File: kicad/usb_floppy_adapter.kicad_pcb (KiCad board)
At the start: 2 copper layers, 48 x 19 mm, 26 parts, among them J1 Conn_02x17_Odd_Even, J2 MICRO_USB_B, J3 Conn_01x02, J4 Conn_01x04, J5 GS2, J6 GS2, J7 GS3, U1 LM1117-3.3, U2 STM32F103C8Tx, U3 USBLC6-2SC6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

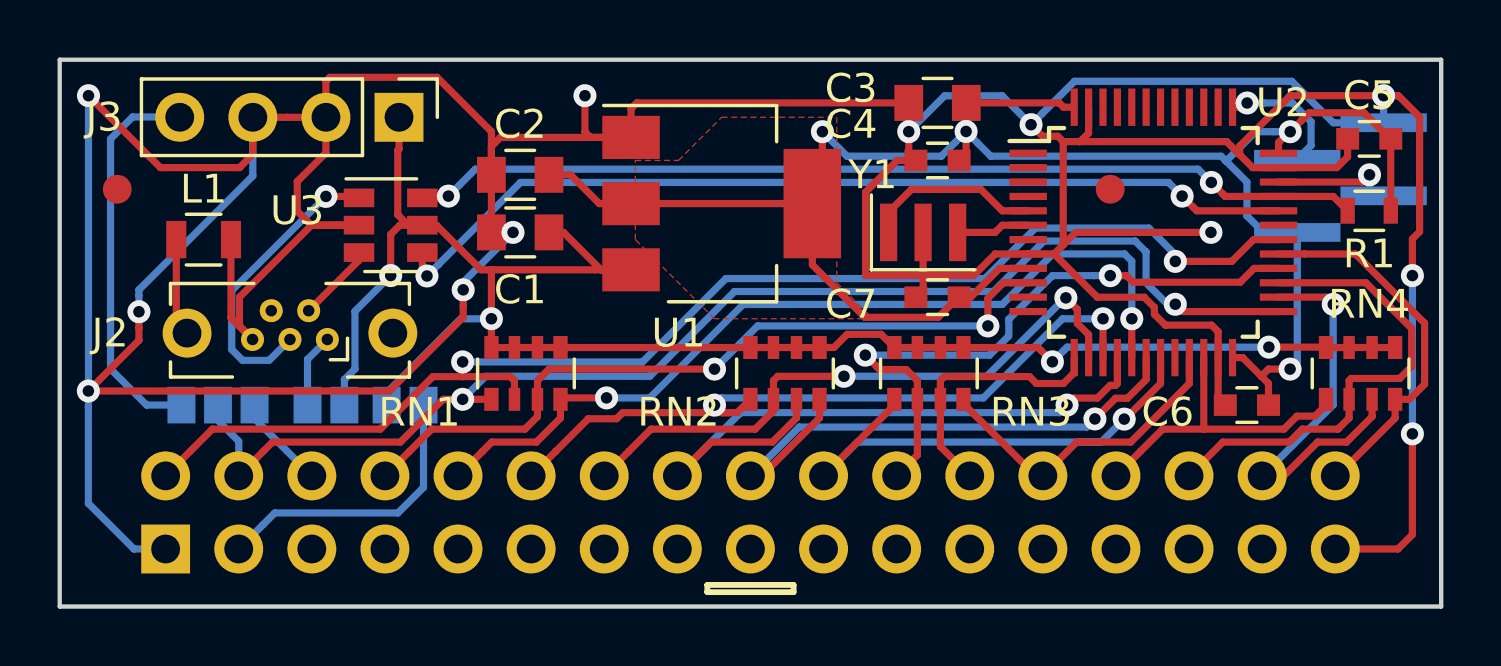
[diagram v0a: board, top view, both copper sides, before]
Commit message: add termination resistors
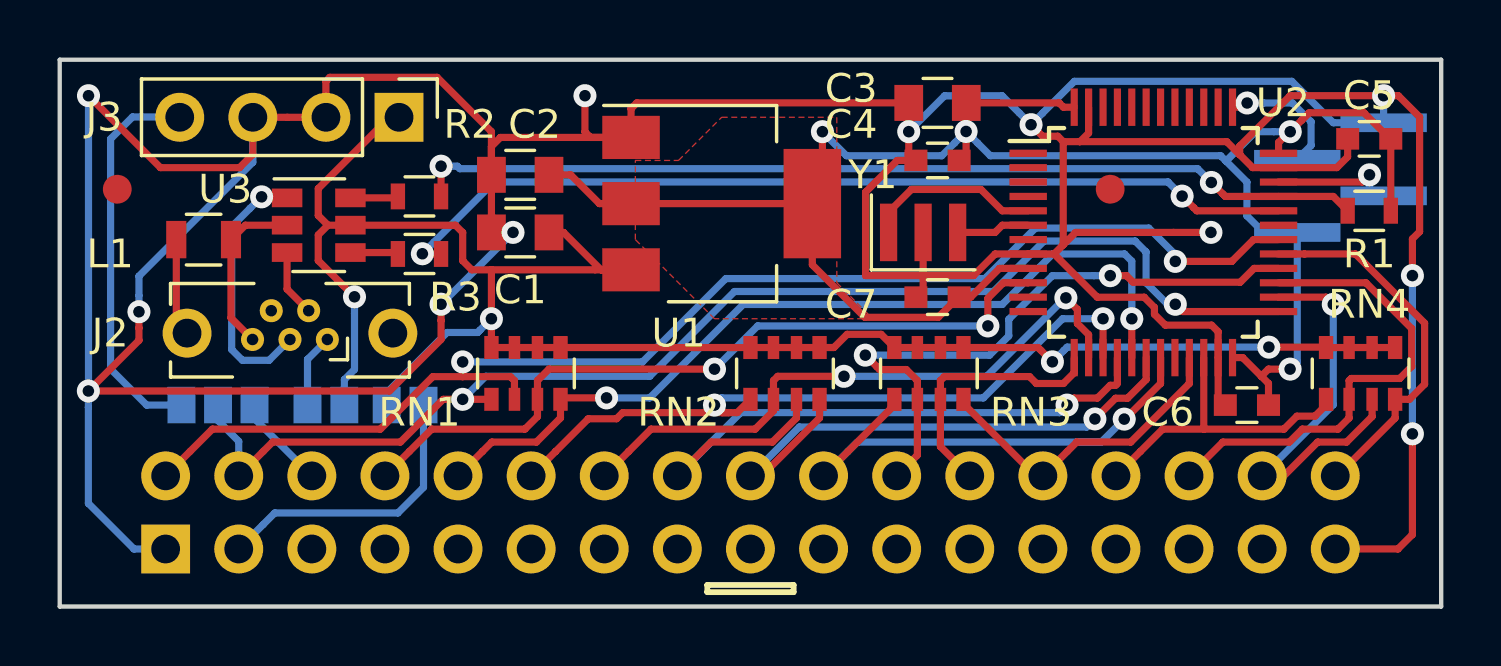
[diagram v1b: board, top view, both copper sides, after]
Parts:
- added R2: 22, Resistors_SMD:R_0603, F.Cu at (134.5, 115.8)
- added R3: 22, Resistors_SMD:R_0603, F.Cu at (134.5, 117.8)
- moved U3 2.50 mm to (131.0, 116.8)
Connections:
- R1 pad 1: /D+ -> Net-(R1-Pad1)
- U2 pad 32: /D- -> Net-(R3-Pad2)
- U2 pad 33: /D+ -> Net-(R1-Pad1)
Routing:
- net Net-(R1-Pad1): track 0.00 -> 33.2 mm, vias 0 -> 2
- net /D+: track 43.5 -> 10.8 mm, vias 3 -> 1
- net Net-(R3-Pad2): track 0.00 -> 31.9 mm, vias 0 -> 2
- net /D-: track 35.0 -> 4.00 mm, vias 2 -> 0
- net GND: track 200.1 -> 189.4 mm
- net +5V: track 63.6 -> 67.5 mm

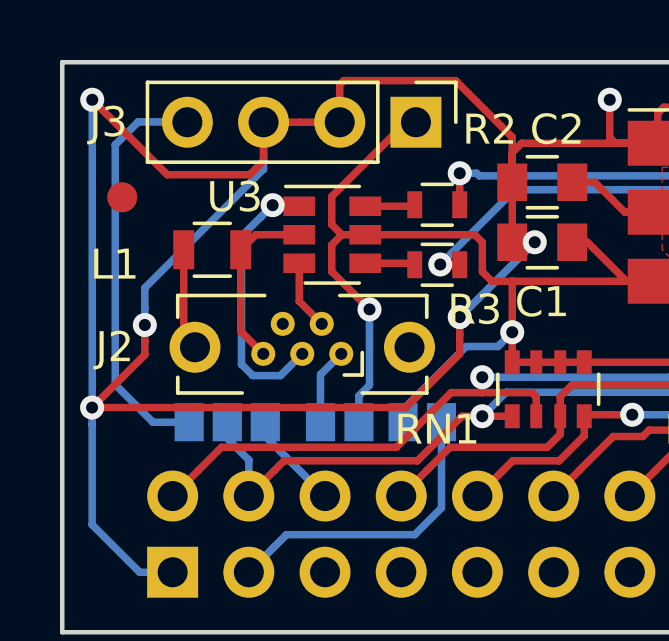
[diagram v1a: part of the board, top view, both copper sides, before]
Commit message: silk screen
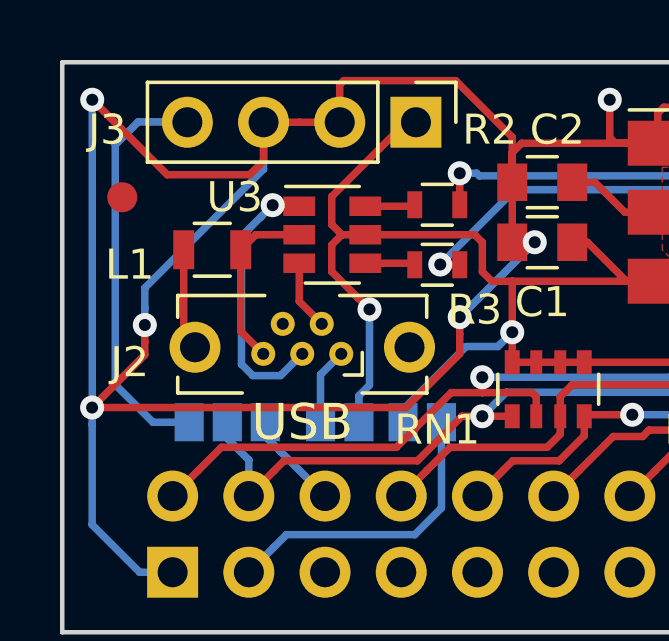
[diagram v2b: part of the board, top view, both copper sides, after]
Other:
- board text added: "12V"
- board text added: "5V"
- board text added: "Design © 2018 B.Freisen"
- board text added: "GND"
- board text added: "USB"
- board text added: "USB FDD Adapter"
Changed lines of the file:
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@@
     (area 121.924999 110.924999 170.075001 130.075001)
     (thickness 1.6)
-    (drawings 12)
+    (drawings 18)
     (tracks 546)
     (zones 0)
@@
     (tags "Micro-USB SMD Typ-B Vertical")
     (attr smd)
-    (fp_text reference J2 (at 6.25 0 180) (layer F.SilkS)
+    (fp_text reference J2 (at 5.75 -0.5 180) (layer F.SilkS)
       (effects (font (size 1 1) (thickness 0.15)))
     )
@@
     (tags "resistor 0805")
     (attr smd)
-    (fp_text reference L1 (at -3.25 0.5) (layer F.SilkS)
+    (fp_text reference L1 (at -2.75 0.5) (layer F.SilkS)
       (effects (font (size 1 1) (thickness 0.15)))
     )
@@
     (descr "Through hole straight pin header, 1x04, 2.54mm pitch, single row")
     (tags "Through hole pin header THT 1x04 2.54mm single row")
-    (fp_text reference J3 (at 0 10.25 360) (layer F.SilkS)
+    (fp_text reference J3 (at 0.25 10.29 360) (layer F.SilkS)
       (effects (font (size 1 1) (thickness 0.15)))
     )
@@
     )
   )
+  (gr_text "Design © 2018 B.Freisen" (at 149.25 115.25) (layer B.SilkS)
+    (effects (font (size 1 1) (thickness 0.15)) (justify mirror))
+  )
+  (gr_text "USB FDD Adapter" (at 149.25 113) (layer B.SilkS)
+    (effects (font (size 1.5 1.5) (thickness 0.3)) (justify mirror))
+  )
+  (gr_text USB (at 130 123) (layer F.SilkS)
+    (effects (font (size 1.2 1.2) (thickness 0.2)))
+  )
+  (gr_text 5V (at 133.75 115.25) (layer B.SilkS)
+    (effects (font (size 1 1) (thickness 0.2)) (justify mirror))
+  )
+  (gr_text GND (at 130 115.25) (layer B.SilkS)
+    (effects (font (size 1 1) (thickness 0.2)) (justify mirror))
+  )
+  (gr_text 12V (at 126.25 115.25) (layer B.SilkS)
+    (effects (font (size 1 1) (thickness 0.2)) (justify mirror))
+  )
   (gr_line (start 144.5 129.5) (end 144.5 129.25) (layer B.SilkS) (width 0.2))
